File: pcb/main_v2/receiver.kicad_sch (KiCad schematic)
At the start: 14 parts, among them IC401 RMS-30+, IC402 HMC374, J401 Conn_Coaxial, J402 Conn_Coaxial

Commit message: updated schematic after review
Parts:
- added C408: 150 pF, Capacitor_SMD:C_0402_1005Metric, symbol Device:C
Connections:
- net filtered Rx: now also C408.1; no longer IC402.3 (IN)
- net Carrier Frequency: Rx renamed Oscillator Rx
- net low filtered Rx 1 renamed f_sdr = 0.9 GHz
- new net filtered Rx 1: C408.2, IC402.3 (IN)
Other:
- note added: "f_c = 1.5 GHz"
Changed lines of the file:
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@@
+		)
+	)
+	(text "f_c = 1.5 GHz"
+		(exclude_from_sim no)
+		(at 119.126 127 90)
+		(effects
+			(font
+				(size 1.27 1.27)
+			)
 		)
 	)
@@
 	(text "Rx Out ->"
 		(exclude_from_sim no)
-		(at 240.538 90.678 0)
+		(at 243.078 84.074 0)
 		(effects
 			(font
@@
 	(wire
 		(pts
+			(xy 153.67 73.66) (xy 170.18 73.66)
+		)
+		(stroke
+			(width 0)
+			(type default)
+		)
+	)
+	(wire
+		(pts
 			(xy 214.63 68.58) (xy 200.66 68.58)
 		)
@@
 	(wire
 		(pts
+			(xy 132.08 73.66) (xy 146.05 73.66)
+		)
+		(stroke
+			(width 0)
+			(type default)
+		)
+	)
+	(wire
+		(pts
 			(xy 198.12 146.05) (xy 218.44 146.05)
 		)
@@
 		(pts
 			(xy 49.53 151.13) (xy 49.53 146.05)
-		)
-		(stroke
-			(width 0)
-			(type default)
-		)
-	)
-	(wire
-		(pts
-			(xy 132.08 73.66) (xy 170.18 73.66)
 		)
 		(stroke
@@
 		)
 	)
+	(label "f_antenne = 2.4 GHz"
+		(at 74.93 73.66 90)
+		(effects
+			(font
+				(size 1.27 1.27)
+			)
+			(justify left bottom)
+		)
+	)
 	(label "downconverted Rx 1"
 		(at 204.47 146.05 90)
@@
 		)
 	)
+	(label "filtered Rx 1"
+		(at 158.75 73.66 270)
+		(fields_autoplaced yes)
+		(effects
+			(font
+				(size 1.27 1.27)
+			)
+			(justify right bottom)
+		)
+		(property "Net Class" "High Speed 50Ohm"
+			(at 160.02 73.66 90)
+			(show_name no)
+			(do_not_autoplace no)
+			(effects
+				(font
+					(size 1.27 1.27)
+					(italic yes)
+				)
+				(justify right)
+			)
+		)
+	)
 	(label "downconverted Rx"
 		(at 44.45 143.51 180)
@@
 		)
 	)
+	(label "f_sdr = 0.9 GHz"
+		(at 248.92 104.14 90)
+		(effects
+			(font
+				(size 1.27 1.27)
+			)
+			(justify left bottom)
+		)
+	)
 	(label "low filtered Rx"
 		(at 217.17 115.57 180)
@@
 		)
 	)
-	(global_label "Carrier Frequency: Rx"
+	(hierarchical_label "Oscillator Rx"
 		(shape input)
-		(at 115.57 137.16 90)
+		(at 115.57 140.97 0)
 		(fields_autoplaced yes)
 		(effects
@@
 			(justify left)
 		)
-		(property "Intersheetrefs" "${INTERSHEET_REFS}"
-			(at 115.57 113.3105 90)
-			(hide yes)
-			(show_name no)
-			(do_not_autoplace no)
-			(effects
-				(font
-					(size 1.27 1.27)
+		(property "Netzklasse" "High Speed 50Ohm"
+			(at 115.57 142.24 0)
+			(show_name no)
+			(do_not_autoplace no)
+			(effects
+				(font
+					(size 1.27 1.27)
+					(italic yes)
 				)
 				(justify left)
@@
 					(unit 1)
 				)
+			)
+		)
+	)
+	(symbol
+		(lib_id "Device:C")
+		(at 149.86 73.66 90)
+		(unit 1)
+		(body_style 1)
+		(exclude_from_sim no)
+		(in_bom yes)
+		(on_board yes)
+		(in_pos_files yes)
+		(dnp no)
+		(property "Reference" "C408"
+			(at 149.86 66.04 90)
+			(show_name no)
+			(do_not_autoplace no)
+			(effects
+				(font
+					(size 1.27 1.27)
+				)
+			)
+		)
+		(property "Value" "150 pF"
+			(at 149.86 68.58 90)
+			(show_name no)
+			(do_not_autoplace no)
+			(effects
+				(font
+					(size 1.27 1.27)
+				)
+			)
+		)
+		(property "Footprint" "Capacitor_SMD:C_0402_1005Metric"
+			(at 153.67 72.6948 0)
+			(hide yes)
+			(show_name no)
+			(do_not_autoplace no)
+			(effects
+				(font
+					(size 1.27 1.27)
+				)
+			)
+		)
+		(property "Datasheet" ""
+			(at 149.86 73.66 0)
+			(hide yes)
+			(show_name no)
+			(do_not_autoplace no)
+			(effects
+				(font
+					(size 1.27 1.27)
+				)
+			)
+		)
+		(property "Description" "Unpolarized capacitor"
+			(at 149.86 73.66 0)
+			(hide yes)
+			(show_name no)
+			(do_not_autoplace no)
+			(effects
+				(font
+					(size 1.27 1.27)
+				)
+			)
+		)
+		(property "Package" "0402"
+			(at 149.86 76.962 90)
+			(show_name no)
+			(do_not_autoplace no)
+			(effects
+				(font
+					(size 1.27 1.27)
+				)
+			)
+		)
+		(property "Voltage" "50 V"
+			(at 149.606 78.74 90)
+			(show_name no)
+			(do_not_autoplace no)
+			(effects
+				(font
+					(size 1.27 1.27)
+				)
+			)
+		)
+		(pin "1"
+		)
+		(pin "2"
+		)
+		(instances
+			(project "main_v2"
+				(path "/0599865e-4bed-44f1-b46e-4b55335b49b2/6cc491e9-db51-4c07-9c5c-0fdbb3f258a1"
+					(reference "C408")
+					(unit 1)
+				)

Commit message: updated schematic
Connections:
- net Rx In renamed f = 2.4 GHz
- net Rx In 1: no longer names the net of C405.2, FL401.1 (IN/OUT)
- net amplified Rx: no longer names the net of C404.1, IC402.6 (OUT), L401.2
- net downconverted Rx 1: no longer names the net of C406.2, FL402.4 (RF_IN)
- net filtered Rx: no longer names the net of C408.1, FL401.4 (_IN/OUT)
- net filtered Rx 1: no longer names the net of C408.2, IC402.3 (IN)
- net lo in: no longer names the net of C403.1, IC401.1 (LO)
- net low filtered Rx: no longer names the net of C407.1, FL402.6 (RF_OUT)
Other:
- note removed: "f_c = 1.5 GHz"
- moved on the sheet: C405, C406, C407, FL401, FL402, J401, J402

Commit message: updarted schematic and simulation
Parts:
- removed J401, J402: Conn_Coaxial, Connector_Coaxial:SMA_Amphenol_132289_EdgeMount, symbol Connector:Conn_Coaxial
- C406, C407: value 10 pF -> 100 pF
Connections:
- net GND: no longer FL402.1 (GROUND_1)
- net amplified Rx: now reaches IC402.6 (OUT), L401.2
- net amplified Rx: now also C404.2; no longer C404.1
- net amplified Rx 1: no longer names the net of IC401.4 (RF)
- net amplified Rx 1: now also C404.1; no longer C404.2
- net downconverted Rx: no longer names the net of C406.1, IC401.5 (IF)
- net f = 2.4 GHz renamed Rx In
- net f_sdr = 0.9 GHz renamed Rx Out
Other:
- note removed: "Rx Out ->"
- note removed: "Rx in ->"
- moved on the sheet: C403, C406, C407, FL402, IC401, L401

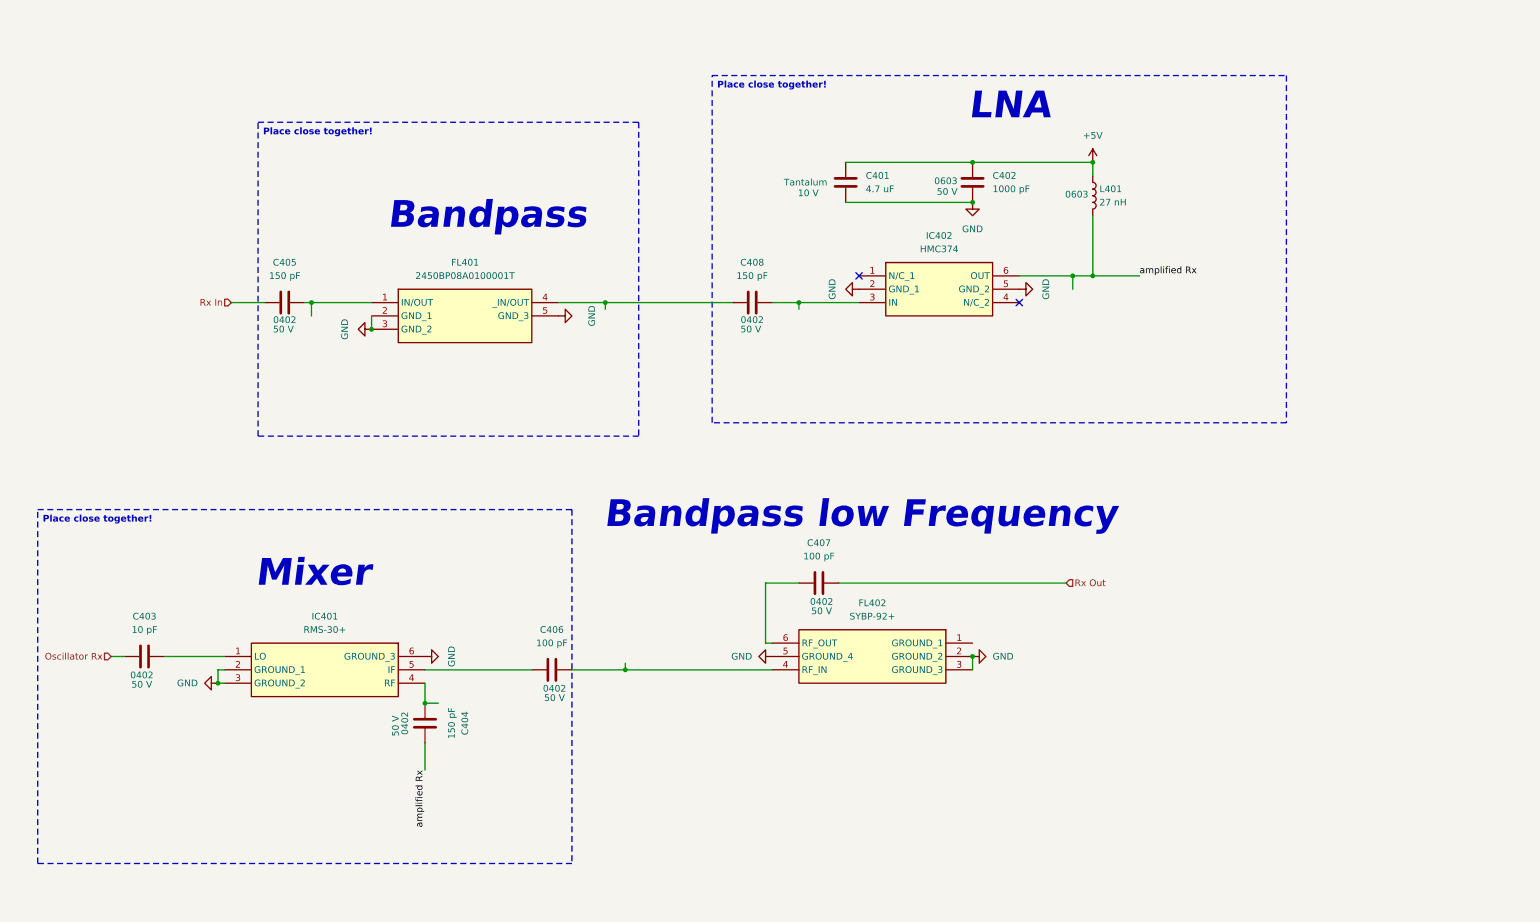
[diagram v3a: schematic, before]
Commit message: updated io schematic
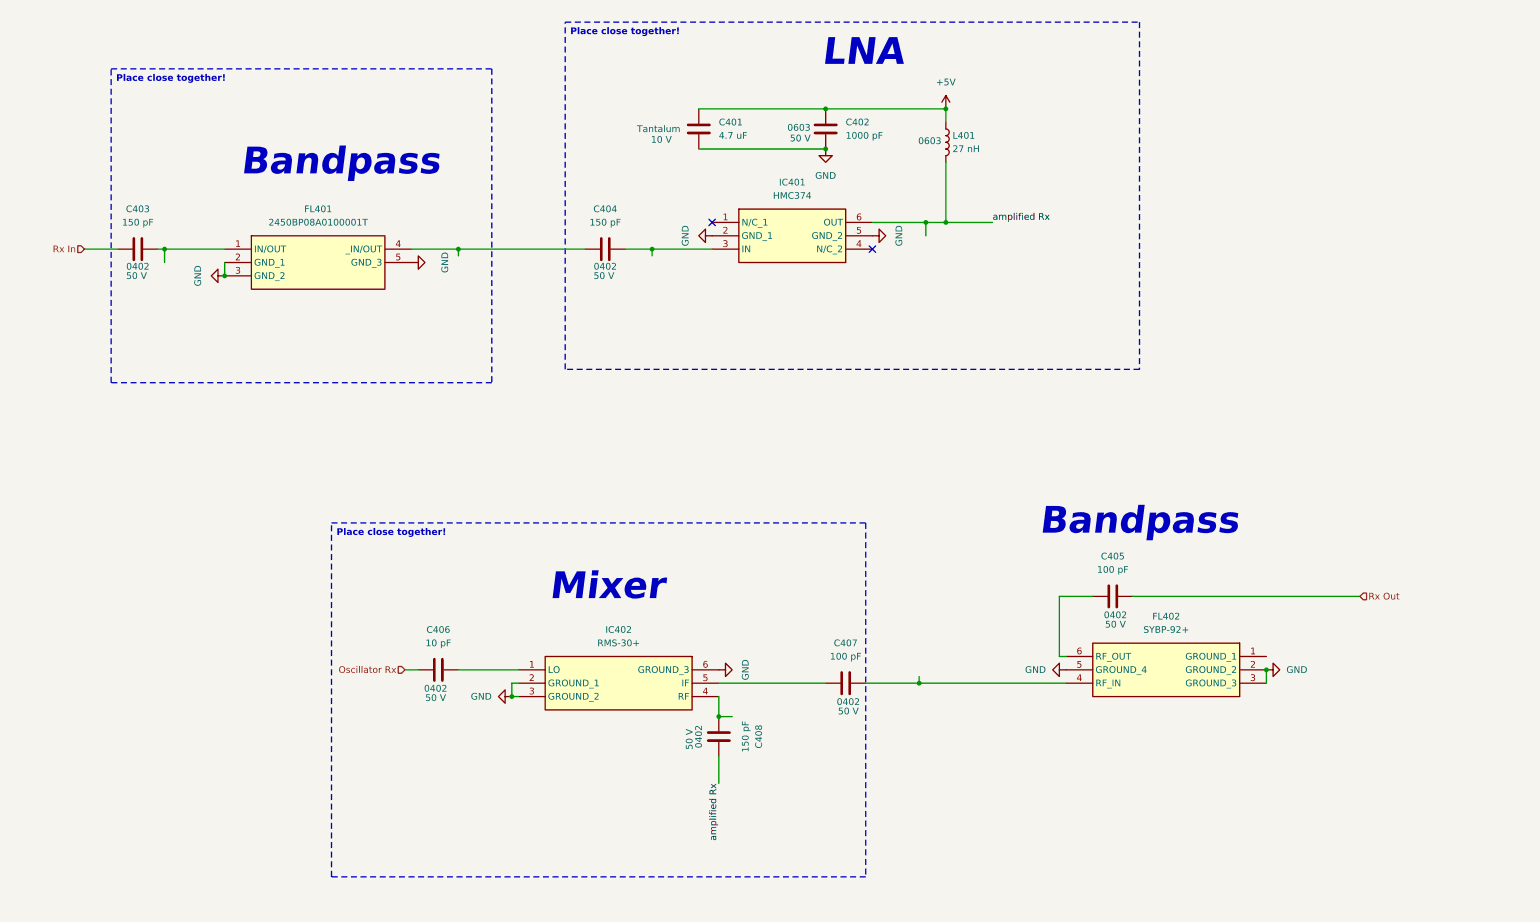
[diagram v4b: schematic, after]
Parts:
- renumbered C405 to C403, C408 to C404, C407 to C405, C403 to C406, C406 to C407, C404 to C408, IC402 to IC401, IC401 to IC402
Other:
- note removed: "Bandpass low Frequency"
- moved on the sheet: C401, C402, C403, C404, C405, C406, C407, C408, FL401, FL402, IC401, IC402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

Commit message: update bom
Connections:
- net GND: now also FL402.1 (GROUND_1)
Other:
- moved on the sheet: C405, C406, C407, C408, FL402, IC402

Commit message: updated layout
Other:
- note added: "TODO:PE45361A-X mit 0.3V am Control Pin"
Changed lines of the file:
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@@
+		)
+	)
+	(text "TODO:PE45361A-X\nmit 0.3V am Control Pin"
+		(exclude_from_sim no)
+		(at 248.412 101.6 0)
+		(effects
+			(font
+				(size 1.27 1.27)
+			)
 		)
 	)

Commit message: finished layout
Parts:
- added C409: 15 pF, Capacitor_SMD:C_0402_1005Metric, symbol Device:C
- added D401: SKY16602-632LF, My Footprints:SKY16602632LF, symbol My Symbols:SKY16602-632LF
- added J401: CONMHF1-SMD-T, My Footprints:CONMHF1SMDT, symbol My Symbols:CONMHF1-SMD-T
- added L402: 12 nH, Inductor_SMD:L_0402_1005Metric, symbol Device:L
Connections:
- net GND: now also D401.3 (GND), J401.2 (GND_1), J401.3 (GND_2), J401.4 (GND_3), L402.2
- net Rx Out: now also D401.2 (RF_OUT); no longer C405.2
- net amplified Rx: now also J401.1 (SIGNAL)
- new net: C409.1, D401.4 (PAD)
- new net: C409.2, L402.1
- new net: C405.2, D401.1 (RF_IN)
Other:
- note added: "Power Clipping"
- note added: "tuned to 1 GHz from datasheet"
- note removed: "TODO:PE45361A-X mit 0.3V am Control Pin"
- moved on the sheet: C405, C406, C407, C408, FL402, IC402
